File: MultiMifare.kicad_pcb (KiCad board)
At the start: 2 copper layers, 54 x 85.6 mm, 5 parts, among them SW1 SW_SPST, SW2 SW_SPST, U1 Mifare_Chip, U2 Mifare_Chip

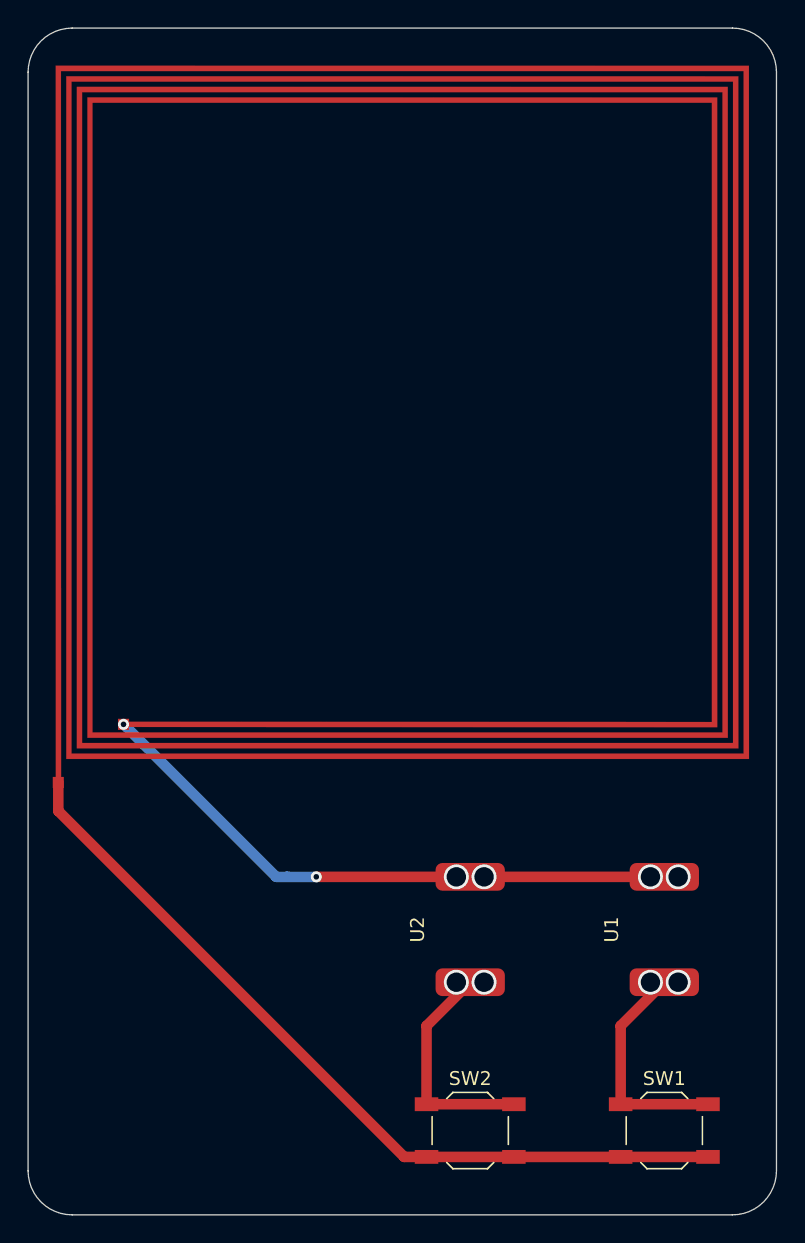
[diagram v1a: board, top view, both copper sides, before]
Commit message: New antenna
50*60mm, 1mm width, 1mm space, 5 turn
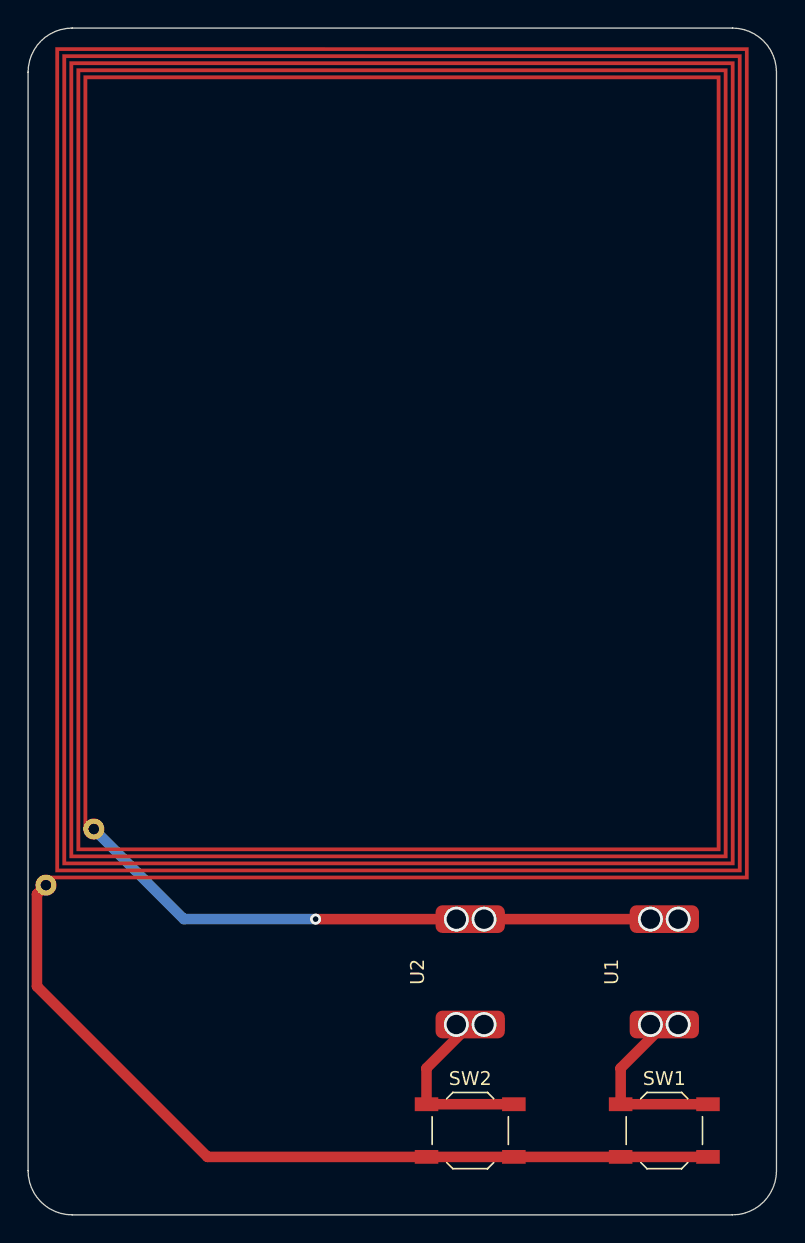
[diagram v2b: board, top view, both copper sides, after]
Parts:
- AE1: footprint MultiMifare:Mifare_Antenna -> MultiMifare:ant_50_60_2400
- moved AE1 3.80 mm to (151.2, 86.4), turned to 0 degrees
- moved U1 3.05 mm to (171.0, 123.0)
- moved U2 3.05 mm to (157.0, 123.0)
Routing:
- net Net-(SW2-Pad1): track 16.4 -> 13.4 mm
- net Net-(SW1-Pad1): track 16.4 -> 13.4 mm
- net Net-(AE1-Pad1): track 59.3 -> 61.1 mm
- net Net-(AE1-Pad2): track 43.6 -> 43.8 mm, vias 6 -> 5
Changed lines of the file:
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@@
     (thickness 1.6)
     (drawings 8)
-    (tracks 29)
+    (tracks 26)
     (zones 0)
     (modules 5)
@@
     (add_net "Net-(SW2-Pad1)")
   )
-  (module MultiMifare:Mifare_Antenna (layer F.Cu)
-    (at 152.1 82.7 90)
-    (fp_text reference AE1 (at 0 0 90) (layer F.SilkS) hide
+  (module MultiMifare:ant_50_60_2400 (layer F.Cu)
+    (at 151.25 86.4)
+    (fp_text reference AE1 (at 0 0) (layer F.SilkS) hide
       (effects (font (size 1.524 1.524) (thickness 0.3)))
     )
-    (fp_text value Antenna_Loop (at 0 3 90) (layer F.SilkS) hide
+    (fp_text value Antenna_Loop (at 0 4.68122) (layer F.SilkS) hide
       (effects (font (size 1.524 1.524) (thickness 0.3)))
     )
-    (fp_poly (pts (xy 25.005773 0.002645) (xy 25.003125 25.003125) (xy 0.002645 25.005773) (xy -24.997834 25.008421)
-      (xy -24.997834 -24.235834) (xy 24.246421 -24.235834) (xy 24.243773 0.002645) (xy 24.241125 24.241125)
-      (xy 0.002645 24.243773) (xy -24.235834 24.246421) (xy -24.235834 -23.473834) (xy 23.484421 -23.473834)
-      (xy 23.481773 0.002645) (xy 23.479125 23.479125) (xy 0.002645 23.481773) (xy -23.473834 23.484421)
-      (xy -23.473834 -22.711834) (xy 22.722421 -22.711834) (xy 22.719773 0.002645) (xy 22.717125 22.717125)
-      (xy 0.002645 22.719773) (xy -22.711834 22.722421) (xy -22.6905 -19.9) (xy -22.3095 -19.9)
-      (xy -22.330834 22.330833) (xy 22.330833 22.330833) (xy 22.330833 -22.341417) (xy -23.08225 -22.341417)
-      (xy -23.08225 23.092833) (xy 23.092833 23.092833) (xy 23.092833 -23.092834) (xy -23.84425 -23.092834)
-      (xy -23.84425 23.854833) (xy 23.854833 23.854833) (xy 23.854833 -23.854834) (xy -24.60625 -23.854834)
-      (xy -24.60625 24.616833) (xy 24.616833 24.616833) (xy 24.616833 -24.616834) (xy -26.4 -24.6095)
-      (xy -26.4 -24.9905) (xy 25.008421 -24.997834) (xy 25.005773 0.002645)) (layer F.Cu) (width 0.01))
-    (fp_line (start -25.2 -25.2) (end 25.2 -25.2) (layer B.CrtYd) (width 0.12))
-    (fp_line (start 25.2 -25.2) (end 25.2 25.2) (layer B.CrtYd) (width 0.12))
-    (fp_line (start 25.2 25.2) (end -25.2 25.2) (layer B.CrtYd) (width 0.12))
-    (fp_line (start -25.2 -25.2) (end -25.2 25.2) (layer B.CrtYd) (width 0.12))
-    (pad 1 smd rect (at -26.692 -24.81 90) (size 0.8 0.8) (layers F.Cu F.Paste F.Mask)
-      (net 3 "Net-(AE1-Pad1)"))
-    (pad 2 smd rect (at -22.5 -20.106 90) (size 0.8 0.8) (layers F.Cu F.Paste F.Mask)
+    (fp_poly (pts (xy 25.831272 -0.029104) (xy 25.828625 -30.030209) (xy 0.828145 -30.032857) (xy -24.172334 -30.035505)
+      (xy -24.172334 29.464) (xy 25.32592 29.464) (xy 25.323272 -0.029104) (xy 25.320625 -29.522209)
+      (xy 0.828145 -29.524857) (xy -23.664334 -29.527505) (xy -23.664334 28.956) (xy 24.81792 28.956)
+      (xy 24.815272 -0.029104) (xy 24.812625 -29.014209) (xy 0.828145 -29.016857) (xy -23.156334 -29.019505)
+      (xy -23.156334 28.448) (xy 24.30992 28.448) (xy 24.307272 -0.029104) (xy 24.304625 -28.506209)
+      (xy 0.828145 -28.508857) (xy -22.648334 -28.511505) (xy -22.648334 27.94) (xy 23.80192 27.94)
+      (xy 23.799272 -0.029104) (xy 23.796625 -27.998209) (xy 0.828145 -28.000857) (xy -22.140334 -28.003505)
+      (xy -22.140334 26.468916) (xy -21.87575 26.468916) (xy -21.87575 -27.738917) (xy 23.537333 -27.738917)
+      (xy 23.537333 27.686) (xy -22.38375 27.686) (xy -22.38375 -28.246917) (xy 24.045333 -28.246917)
+      (xy 24.045333 28.194) (xy -22.89175 28.194) (xy -22.89175 -28.754917) (xy 24.553333 -28.754917)
+      (xy 24.553333 28.702) (xy -23.39975 28.702) (xy -23.39975 -29.262917) (xy 25.061333 -29.262917)
+      (xy 25.061333 29.21) (xy -23.90775 29.21) (xy -23.90775 -29.770917) (xy 25.569333 -29.770917)
+      (xy 25.569333 29.718) (xy -25.146 29.718) (xy -25.146 29.972) (xy 25.83392 29.972)
+      (xy 25.831272 -0.029104)) (layer F.Cu) (width 0.01))
+    (pad 2 thru_hole circle (at -21.4 26.35) (size 1.524 1.524) (drill 0.762) (layers *.Cu *.Mask)
       (net 4 "Net-(AE1-Pad2)"))
+    (pad 1 thru_hole circle (at -24.85 30.4) (size 1.524 1.524) (drill 0.762) (layers *.Cu *.Mask)
+      (net 3 "Net-(AE1-Pad1)"))
   )
   (module MultiMifare:Mifare_Chip (layer F.Cu)
-    (at 157 120 270)
+    (at 157 123.05 270)
     (fp_text reference U2 (at 0 3.8 90) (layer F.SilkS)
       (effects (font (size 1 1) (thickness 0.15)))
@@
   )
   (module MultiMifare:Mifare_Chip (layer F.Cu)
-    (at 171 120 270)
+    (at 171 123.05 270)
     (fp_text reference U1 (at 0 3.8 90) (layer F.SilkS)
       (effects (font (size 1 1) (thickness 0.15)))
@@
   (gr_line (start 179.09 58.16) (end 179.09 137.4) (layer Edge.Cuts) (width 0.05))
   (gr_line (start 128.29 54.98) (end 175.91 54.98) (layer Edge.Cuts) (width 0.05))
-  (via (at 172 123.8) (size 1.8) (drill 1.4) (layers F.Cu B.Cu) (net 1))
-  (via (at 170 123.8) (size 1.8) (drill 1.4) (layers F.Cu B.Cu) (net 1))
-  (via (at 156 123.8) (size 1.8) (drill 1.4) (layers F.Cu B.Cu) (net 2))
-  (via (at 158 123.8) (size 1.8) (drill 1.4) (layers F.Cu B.Cu) (net 2))
-  (via (at 172 116.2) (size 1.8) (drill 1.4) (layers F.Cu B.Cu) (net 4))
-  (via (at 170 116.2) (size 1.8) (drill 1.4) (layers F.Cu B.Cu) (net 4))
-  (via (at 158 116.2) (size 1.8) (drill 1.4) (layers F.Cu B.Cu) (net 4))
+  (via (at 172 126.85) (size 1.8) (drill 1.4) (layers F.Cu B.Cu) (net 1))
+  (via (at 170 126.85) (size 1.8) (drill 1.4) (layers F.Cu B.Cu) (net 1))
   (segment (start 174.15 132.6) (end 167.85 132.6) (width 0.762) (layer F.Cu) (net 1))
-  (segment (start 167.85 126.95) (end 171 123.8) (width 0.762) (layer F.Cu) (net 1))
-  (segment (start 167.85 132.6) (end 167.85 126.95) (width 0.762) (layer F.Cu) (net 1))
+  (segment (start 167.85 130) (end 171 126.85) (width 0.762) (layer F.Cu) (net 1))
+  (segment (start 167.85 132.6) (end 167.85 130) (width 0.762) (layer F.Cu) (net 1))
+  (via (at 156 126.85) (size 1.8) (drill 1.4) (layers F.Cu B.Cu) (net 2))
+  (via (at 158 126.85) (size 1.8) (drill 1.4) (layers F.Cu B.Cu) (net 2))
   (segment (start 160.15 132.6) (end 153.85 132.6) (width 0.762) (layer F.Cu) (net 2))
-  (segment (start 153.85 126.95) (end 157 123.8) (width 0.762) (layer F.Cu) (net 2))
-  (segment (start 153.85 132.6) (end 153.85 126.95) (width 0.762) (layer F.Cu) (net 2))
+  (segment (start 153.85 130) (end 157 126.85) (width 0.762) (layer F.Cu) (net 2))
+  (segment (start 153.85 132.6) (end 153.85 130) (width 0.762) (layer F.Cu) (net 2))
   (segment (start 174.15 136.4) (end 167.85 136.4) (width 0.762) (layer F.Cu) (net 3))
   (segment (start 167.85 136.4) (end 160.15 136.4) (width 0.762) (layer F.Cu) (net 3))
-  (segment (start 153.85 136.4) (end 152.238 136.4) (width 0.762) (layer F.Cu) (net 3))
   (segment (start 160.15 136.4) (end 153.85 136.4) (width 0.762) (layer F.Cu) (net 3))
-  (segment (start 152.238 136.4) (end 127.29 111.452) (width 0.762) (layer F.Cu) (net 3))
-  (segment (start 127.29 111.452) (end 127.29 109.392) (width 0.762) (layer F.Cu) (net 3))
-  (via (at 131.994 105.2) (size 0.8) (drill 0.4) (layers F.Cu B.Cu) (net 4))
-  (via (at 145.9 116.2) (size 0.8) (drill 0.4) (layers F.Cu B.Cu) (net 4))
-  (segment (start 143.788 116.2) (end 145.9 116.2) (width 0.762) (layer B.Cu) (net 4))
-  (segment (start 132 105.2) (end 131.994 105.2) (width 0.762) (layer B.Cu) (net 4))
-  (segment (start 143 116.2) (end 132 105.2) (width 0.762) (layer B.Cu) (net 4))
-  (segment (start 143.8 116.2) (end 143 116.2) (width 0.762) (layer B.Cu) (net 4))
-  (segment (start 171 116.2) (end 157 116.2) (width 0.762) (layer F.Cu) (net 4))
-  (segment (start 157 116.2) (end 156 116.2) (width 0.762) (layer F.Cu) (net 4))
-  (segment (start 156 116.2) (end 145.9 116.2) (width 0.762) (layer F.Cu) (net 4))
-  (via (at 156 116.2) (size 1.8) (drill 1.4) (layers F.Cu B.Cu) (net 4))
+  (segment (start 125.75 117.45) (end 126.4 116.8) (width 0.762) (layer F.Cu) (net 3))
+  (segment (start 125.75 124.1) (end 125.75 117.45) (width 0.762) (layer F.Cu) (net 3))
+  (segment (start 138.05 136.4) (end 125.75 124.1) (width 0.762) (layer F.Cu) (net 3))
+  (segment (start 153.85 136.4) (end 138.05 136.4) (width 0.762) (layer F.Cu) (net 3))
+  (via (at 172 119.25) (size 1.8) (drill 1.4) (layers F.Cu B.Cu) (net 4))
+  (via (at 170 119.25) (size 1.8) (drill 1.4) (layers F.Cu B.Cu) (net 4))
+  (via (at 158 119.25) (size 1.8) (drill 1.4) (layers F.Cu B.Cu) (net 4))
+  (via (at 156 119.25) (size 1.8) (drill 1.4) (layers F.Cu B.Cu) (net 4))
+  (segment (start 171 119.25) (end 157 119.25) (width 0.762) (layer F.Cu) (net 4))
+  (via (at 145.85 119.25) (size 0.8) (drill 0.4) (layers F.Cu B.Cu) (net 4))
+  (segment (start 157 119.25) (end 145.85 119.25) (width 0.762) (layer F.Cu) (net 4))
+  (segment (start 145.85 119.25) (end 136.35 119.25) (width 0.762) (layer B.Cu) (net 4))
+  (segment (start 136.35 119.25) (end 129.85 112.75) (width 0.762) (layer B.Cu) (net 4))
 )
